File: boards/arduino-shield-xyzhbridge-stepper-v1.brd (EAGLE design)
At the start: 73.7 x 55.5 mm, 21 parts, among them IC1 2967-MP6500, IC3 2967-MP6500, J4 ARDUINO_R3_SHIELD, J9 455-1750-1-ND

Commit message: finishing touches on a draft of the full control board with slimezistor etc
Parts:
- added J5: 455-1750-1-ND, SparkFun-Connectors:1X03
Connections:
- new net N$9: J4.A4, J5.2
- net 5V: now also J5.3
- net GND: now also J5.1
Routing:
- net N$9: track 0.00 -> 47.6 mm
- net 5V: track 228.2 -> 246.5 mm
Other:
- board text added: "A"
- board text added: "A1"
- board text added: "A2"
- board text added: "A3"
- board text added: "B"
- board text added: "SlimeZistor"
- board text removed: "slimezistor"
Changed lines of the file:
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@@
 <text x="4.826" y="24.257" size="1.27" layer="21">Vext</text>
 <text x="69.85" y="51.181" size="1.27" layer="21" rot="R270">MOTOR1</text>
-<text x="70.104" y="22.225" size="1.27" layer="21" rot="R270">MOTOR3</text>
-<text x="68.834" y="25.4" size="1.27" layer="21" rot="R180">Pololu
+<text x="68.834" y="22.225" size="1.27" layer="21" rot="R270">MOTOR3</text>
+<text x="57.404" y="43.815" size="1.27" layer="21" rot="R180">Pololu
 2966</text>
 <text x="70.993" y="28.829" size="1.27" layer="21" rot="R90">MOTOR2</text>
@@
 <text x="28.956" y="27.432" size="1.27" layer="21">VM2</text>
 <text x="39.116" y="25.527" size="1.27" layer="21">VM3</text>
-<text x="23.876" y="14.097" size="1.27" layer="21">slimezistor</text>
-<text x="20.066" y="12.192" size="1.27" layer="21">Cs</text>
+<text x="19.431" y="12.192" size="1.27" layer="21">Cs</text>
 <text x="11.176" y="8.382" size="1.27" layer="21">10uF</text>
 <text x="10.541" y="19.812" size="1.27" layer="21">10uF</text>
+<text x="27.051" y="16.637" size="1.27" layer="21">A1</text>
+<text x="21.336" y="14.732" size="1.27" layer="21">A2</text>
+<text x="23.876" y="14.097" size="1.27" layer="21">SlimeZistor</text>
+<text x="71.12" y="20.574" size="1.27" layer="21">A</text>
+<text x="71.12" y="15.494" size="1.27" layer="21">B</text>
+<text x="9.271" y="6.477" size="1.27" layer="21">A3</text>
+<text x="4.826" y="1.397" size="1.27" layer="21">GND</text>
+<text x="12.446" y="1.397" size="1.27" layer="21">5V</text>
 </plain>
 <attributes>
@@
 <attribute name="VALUE" x="17.78" y="25.146" size="0.6096" layer="27" font="vector" ratio="20" align="top-left"/>
 </element>
+<element name="J5" library="SparkFun-Connectors" package="1X03" value="455-1750-1-ND" x="7.62" y="4.445" smashed="yes">
+<attribute name="NAME" x="6.35" y="5.842" size="0.6096" layer="25" font="vector" ratio="20"/>
+<attribute name="PROD_ID" value="XXX-00000" x="7.62" y="4.445" size="1.778" layer="27" display="off"/>
+<attribute name="VALUE" x="6.35" y="2.413" size="0.6096" layer="27" font="vector" ratio="20"/>
+</element>
 </elements>
 <signals>
@@
 <wire x1="15.875" y1="12.065" x2="18.415" y2="12.065" width="0.508" layer="16"/>
 <contactref element="J6" pad="3"/>
-<wire x1="46.99" y1="35.56" x2="62.23" y2="35.56" width="0" layer="19" extent="1-1"/>
-<wire x1="35.56" y1="48.26" x2="46.99" y2="35.56" width="0" layer="19" extent="1-1"/>
-<wire x1="30.48" y1="30.48" x2="46.99" y2="35.56" width="0" layer="19" extent="1-1"/>
-<wire x1="27.94" y1="30.48" x2="30.48" y2="30.48" width="0" layer="19" extent="1-1"/>
-<wire x1="17.78" y1="53.34" x2="35.56" y2="48.26" width="0" layer="19" extent="1-1"/>
-<wire x1="60.96" y1="15.875" x2="62.23" y2="35.56" width="0" layer="19" extent="1-1"/>
-<wire x1="45.72" y1="15.875" x2="60.96" y2="15.875" width="0" layer="19" extent="1-1"/>
-<wire x1="34.29" y1="5.08" x2="45.72" y2="15.875" width="0" layer="19" extent="1-1"/>
-<wire x1="31.75" y1="5.08" x2="34.29" y2="5.08" width="0" layer="19" extent="1-1"/>
-<wire x1="18.415" y1="12.065" x2="31.75" y2="5.08" width="0" layer="19" extent="1-1"/>
-<wire x1="5.715" y1="46.355" x2="15.875" y2="12.065" width="0" layer="19" extent="1-1"/>
-<wire x1="73.66" y1="2.54" x2="60.96" y2="15.875" width="0" layer="19" extent="1-1"/>
-<wire x1="6.35" y1="30.226" x2="15.875" y2="12.065" width="0" layer="19" extent="1-1"/>
+<contactref element="J5" pad="1"/>
 </signal>
 <signal name="N$30">
@@
 <wire x1="58.42" y1="28.575" x2="60.96" y2="28.575" width="0.508" layer="1"/>
 <contactref element="U$1" pad="VCC"/>
-<wire x1="29.21" y1="5.08" x2="29.21" y2="19.685" width="0.508" layer="1"/>
+<wire x1="29.21" y1="5.08" x2="29.21" y2="8.89" width="0.508" layer="1"/>
+<wire x1="29.21" y1="8.89" x2="29.21" y2="19.685" width="0.508" layer="1"/>
 <wire x1="29.21" y1="19.685" x2="29.845" y2="20.32" width="0.508" layer="1"/>
 <wire x1="29.845" y1="20.32" x2="29.845" y2="22.86" width="0.508" layer="1"/>
@@
 <wire x1="5.715" y1="48.895" x2="8.89" y2="48.895" width="0.508" layer="16"/>
 <wire x1="8.89" y1="48.895" x2="20.32" y2="37.465" width="0.508" layer="16"/>
+<contactref element="J5" pad="3"/>
+<wire x1="12.7" y1="4.445" x2="17.145" y2="8.89" width="0.508" layer="1"/>
+<wire x1="17.145" y1="8.89" x2="29.21" y2="8.89" width="0.508" layer="1"/>
 </signal>
 <signal name="PWMB">
@@
 <wire x1="12.7" y1="43.815" x2="12.7" y2="53.34" width="0.508" layer="1"/>
 </signal>
+<signal name="N$9">
+<contactref element="J4" pad="A4"/>
+<contactref element="J5" pad="2"/>
+<wire x1="10.16" y1="4.445" x2="10.16" y2="1.905" width="0.508" layer="16"/>
+<wire x1="10.16" y1="1.905" x2="52.07" y2="1.905" width="0.508" layer="16"/>
+<wire x1="52.07" y1="1.905" x2="52.07" y2="5.08" width="0.508" layer="16"/>
+</signal>
 </signals>

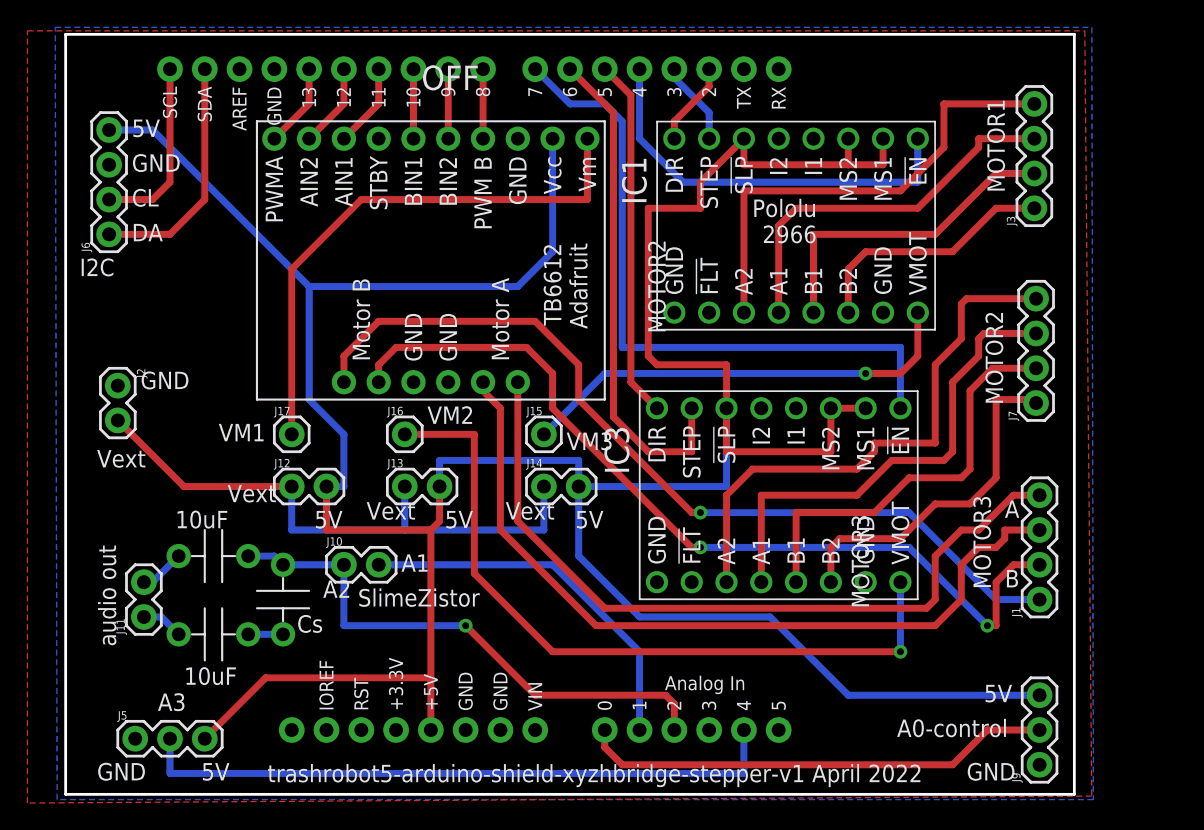
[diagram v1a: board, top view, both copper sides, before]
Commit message: two new boards, xyz and slime and xyzhbridge and slime
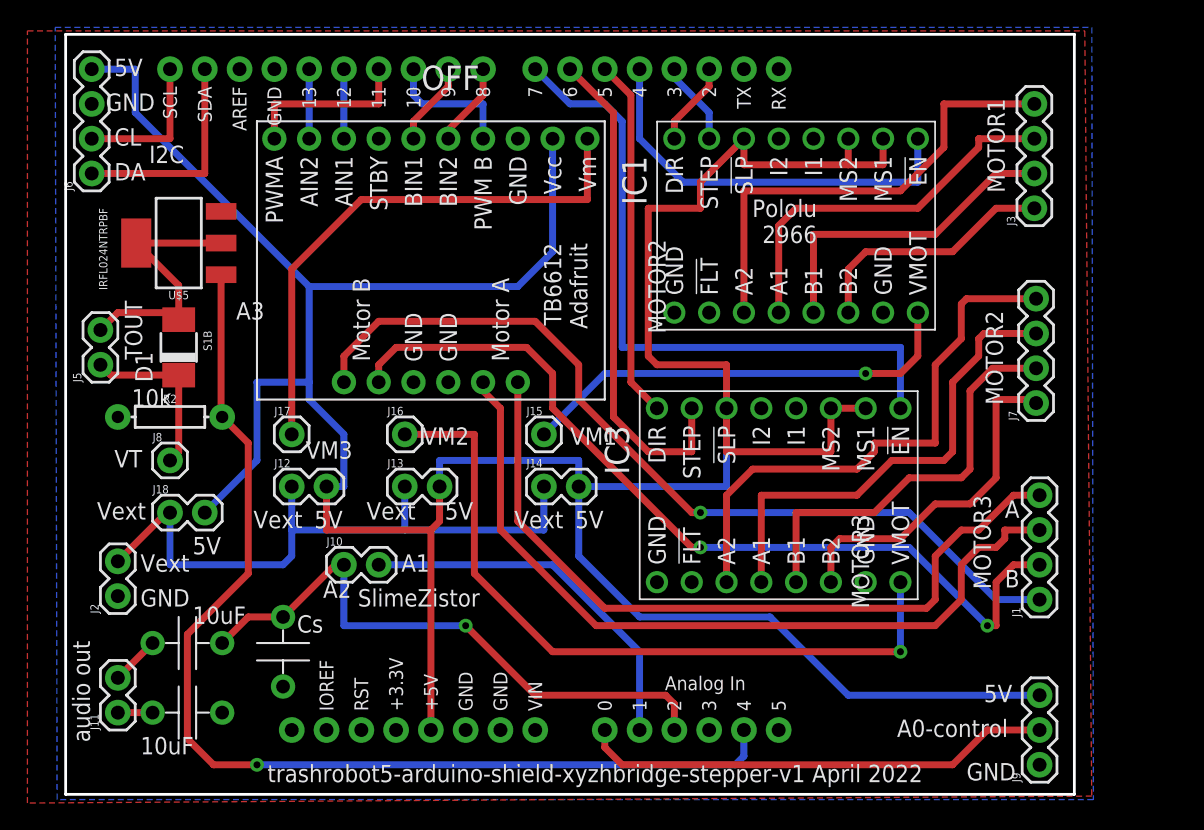
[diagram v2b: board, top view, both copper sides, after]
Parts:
- added D1: (no value), diode:DO-214AC
- added J18: (no value), SparkFun-Connectors:1X02
- added J8: (no value), SparkFun-Connectors:1X01
- added R2: (no value), SparkFun-Resistors:AXIAL-0.3
- added U$5: IRFL024NPBF, spietz-library-2:SOT223
- J5: value 455-1750-1-ND -> (none); device SparkFun-Connectors:1X03 -> SparkFun-Connectors:1X02
- moved J5 27.4 mm to (5.08, 31.8), turned to 90 degrees
- moved J2 15.4 mm to (6.35, 14.9), turned to 90 degrees
- moved J11 7.24 mm to (6.35, 6.35)
- moved U$4 6.63 mm to (11.4, 11.4)
- moved U$2 6.02 mm to (11.4, 6.35)
- moved J6 4.62 mm to (4.45, 45.7)
- moved U$3 3.81 mm to (18.4, 10.8)
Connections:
- removed net N$9: J4.A4, J5.2
- new net A3: J4.A4, R2.P$2, U$5.1
- new net N$18: D1.A, J5.2, U$5.2, U$5.4
- new net VTRANSISTOR: D1.C, J5.1, J8.1
- net 5V: now also J18.2; no longer J5.3
- net AIN1: now also J4.D12; no longer J4.D11
- net AIN2: now also J4.D13; no longer J4.D12
- net BIN1: now also J4.D9; no longer J4.D10
- net BIN2: now also J4.D8; no longer J4.D9
- net EXT: now also J18.1
- net GND: now also R2.P$1, U$5.3; no longer J5.1
- net PWMA: now also J4.D11; no longer J4.D13
- net PWMB: now also J4.D10; no longer J4.D8
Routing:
- net A3: track 0.00 -> 80.1 mm, vias 0 -> 1
- net N$9: track 47.6 -> 0.00 mm
- net N$18: track 0.00 -> 19.3 mm
- net VTRANSISTOR: track 0.00 -> 12.5 mm
- net PWMA: track 6.13 -> 12.7 mm
- net EXT: track 42.6 -> 48.1 mm
- net PWMB: track 5.08 -> 9.79 mm
- net A2: track 40.1 -> 44.1 mm
- net GND: track 2.54 -> 0.00 mm
- net SCL: track 13.2 -> 10.8 mm
- net SDA: track 17.6 -> 15.9 mm
- net 5V: track 246.5 -> 248.0 mm
- net BIN2: track 5.08 -> 6.13 mm
- net BIN1: track 5.08 -> 6.13 mm
- net AIN2: track 6.13 -> 5.08 mm
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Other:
- board text added: "10k"
- board text added: "IRFL024NTRPBF"
- board text added: "S1B"
- board text added: "TOUT"
- board text added: "VT"
